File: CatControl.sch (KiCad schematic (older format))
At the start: 4 parts, among them J2 CAT, U2 FT232RL

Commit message: Replace 100 uF caps
The ones I had selected before were only rated for 4V, and I need at least 5V (USB bus).
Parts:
- C16: Manufacturer_Part_Number TPST107M004R0500 -> TACT107M006XTA; Price 0.93 -> 4.4; Vendor Part Number 581-TPST107M004R0500 -> 581-TACT107M006XTA
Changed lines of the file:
@@
 F 1 "100μF" H 5965 1855 50 0000 L CNN
 F 2 "Capacitor_SMD:C_1210_3225Metric" H 5888 1750 50 0001 C CNN
-F 3 "https://www.mouser.com/datasheet/2/40/TPS-2066671.pdf" H 5850 1900 50 0001 C CNN
+F 3 "https://www.mouser.com/datasheet/2/40/tac-776418.pdf" H 5850 1900 50 0001 C CNN
 F 4 "AVX" H 5965 2046 50 0001 C CNN "Manufacturer_Name"
-F 5 "TPST107M004R0500" H 5965 2046 50 0001 C CNN "Manufacturer_Part_Number"
-F 6 "0.93" H 5965 2046 50 0001 C CNN "Price"
-F 7 "581-TPST107M004R0500" H 5965 2046 50 0001 C CNN "Vendor Part Number"
+F 5 "TACT107M006XTA" H 5965 2046 50 0001 C CNN "Manufacturer_Part_Number"
+F 6 "4.4" H 5965 2046 50 0001 C CNN "Price"
+F 7 "581-TACT107M006XTA" H 5965 2046 50 0001 C CNN "Vendor Part Number"
 F 8 "Mouser" H 5965 2046 50 0001 C CNN "Vendor"
 	1    5850 1900

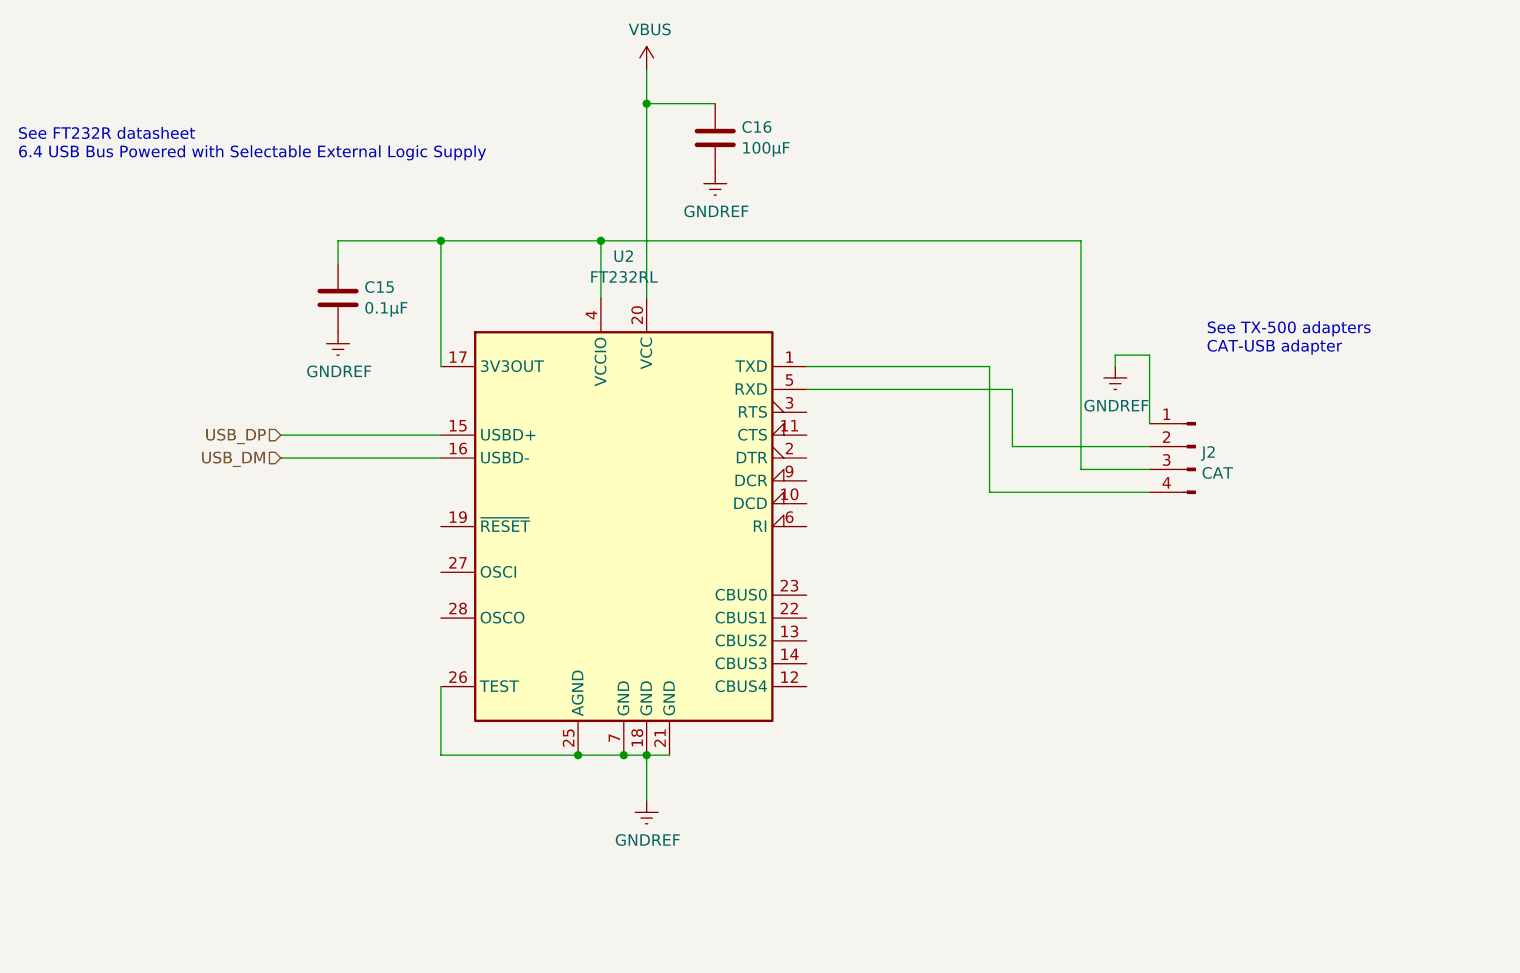
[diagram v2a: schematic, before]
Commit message: Add ID markings on schema and pcb
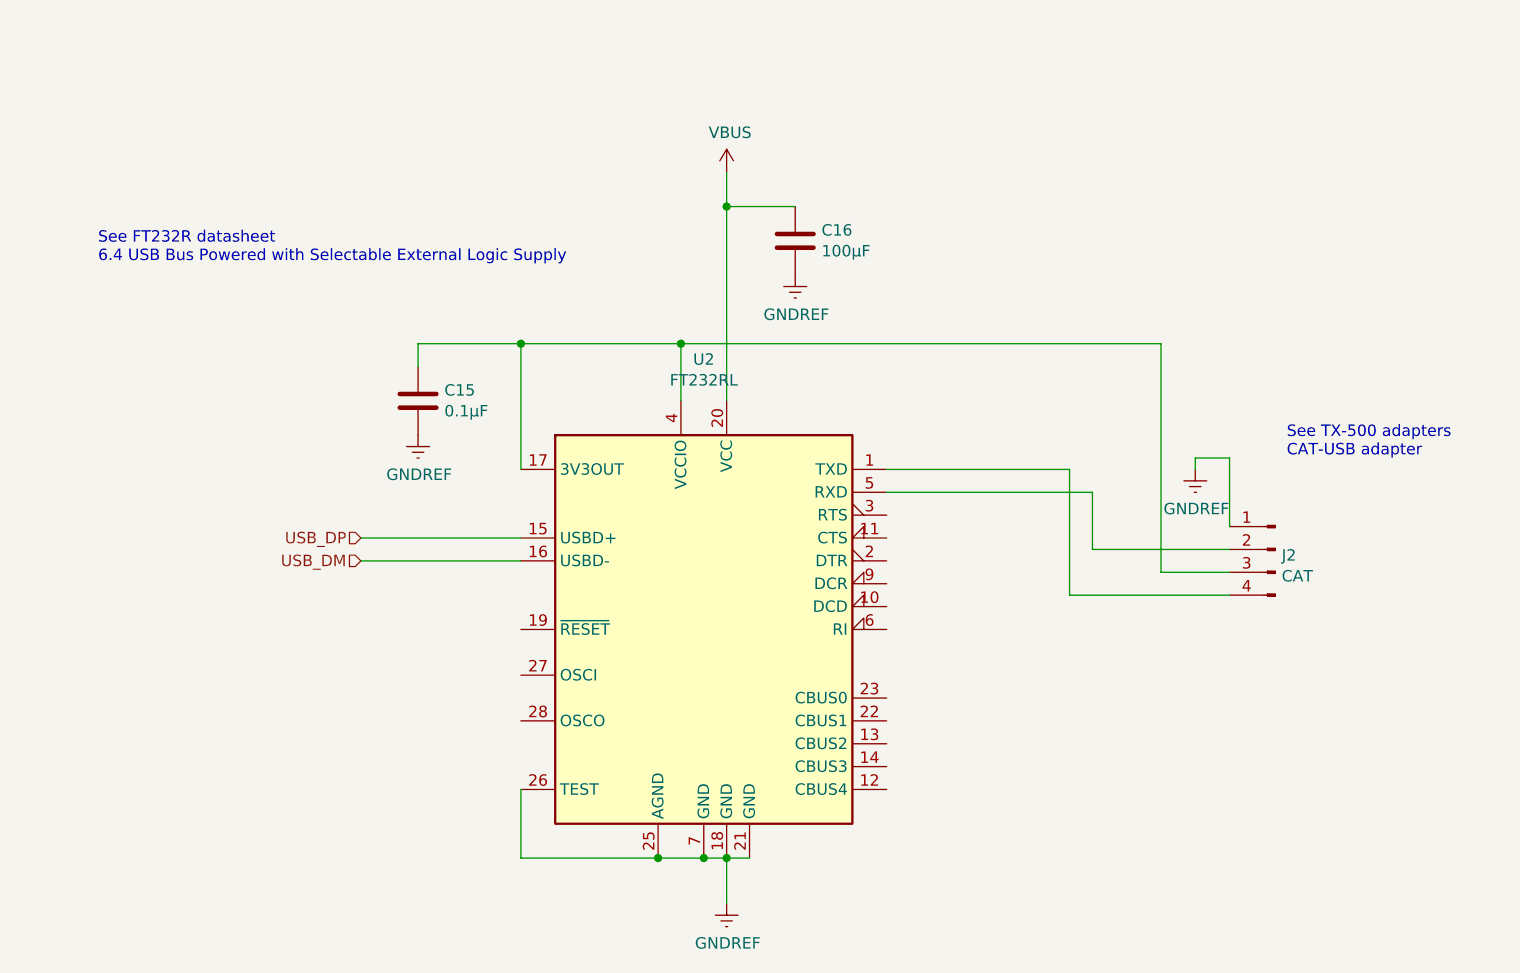
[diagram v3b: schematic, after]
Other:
- moved on the sheet: C15, C16, J2, U2

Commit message: First pass at routing PCB
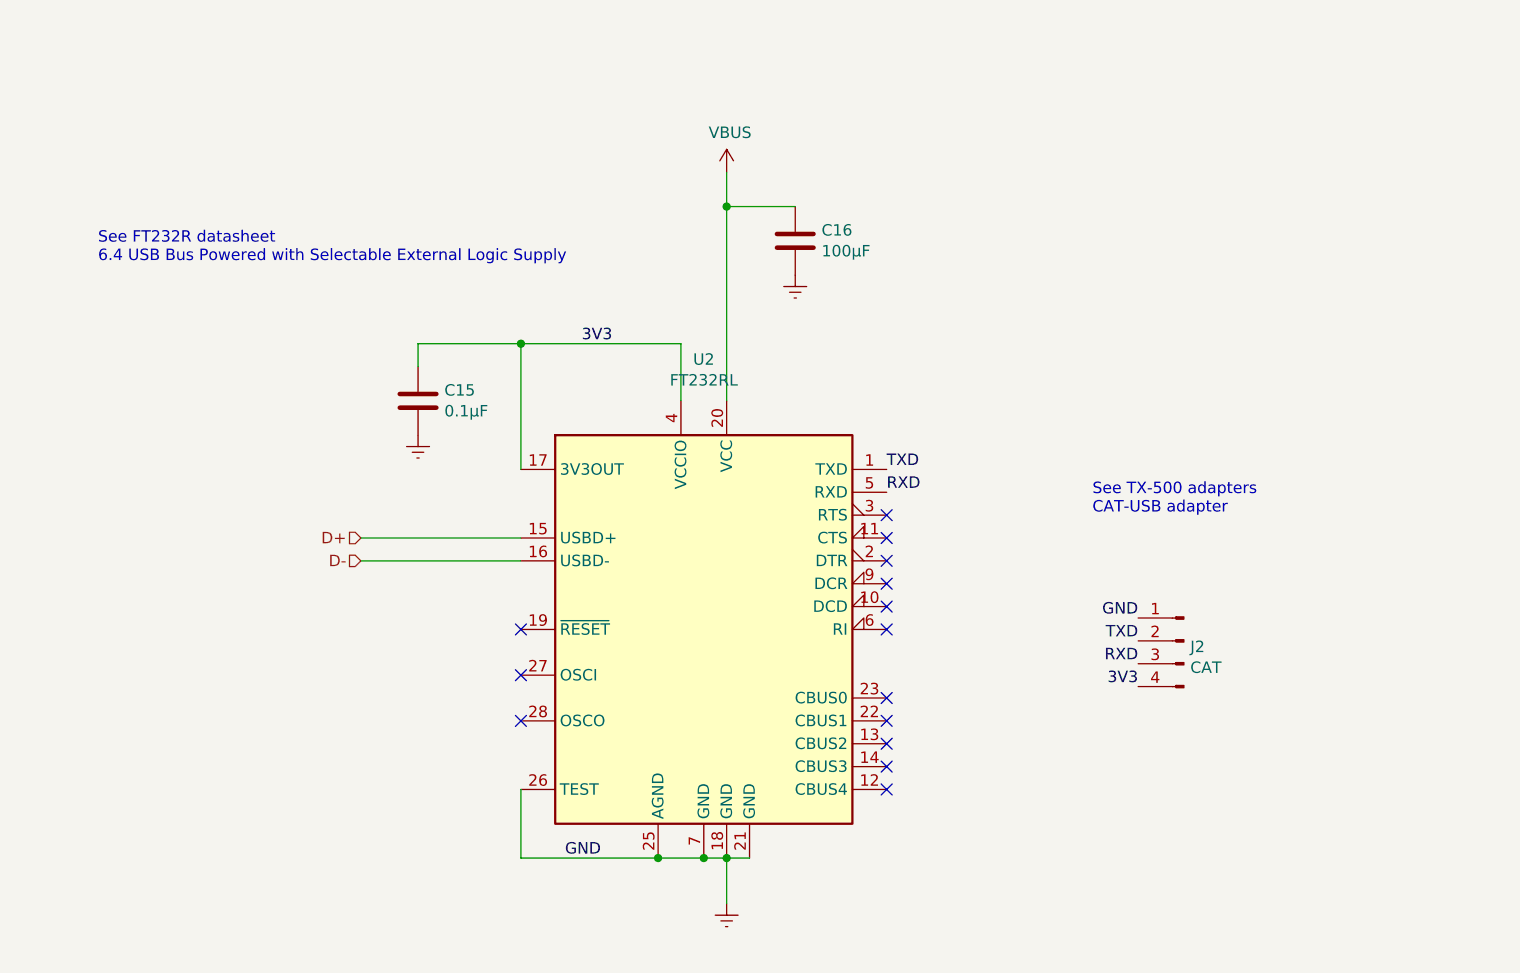
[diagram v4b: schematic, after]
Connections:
- net 3V3: now reaches C15.1, U2.17 (3V3OUT), U2.4 (VCCIO)
- net 3V3: now also J2.4 (Pin_4); no longer J2.3 (Pin_3)
- net TXD: now reaches U2.1 (TXD)
- net TXD: now also J2.2 (Pin_2); no longer J2.4 (Pin_4)
- net RXD: now reaches U2.5 (RXD)
- net RXD: now also J2.3 (Pin_3); no longer J2.2 (Pin_2)
- net USB_DM renamed D-
- net USB_DP renamed D+
- no-connect marks 0 -> 14
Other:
- moved on the sheet: J2
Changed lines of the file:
@@
 Rev "0.1"
 Comp "Chris Keller K0SWE"
-Comment1 ""
+Comment1 "Licensed under Apache-2.0"
 Comment2 ""
 Comment3 ""
@@
 L Connector:Conn_01x04_Male J?
 U 1 1 605A84FC
-P 8300 3700
+P 7900 4100
 AR Path="/605A84FC" Ref="J?"  Part="1"
 AR Path="/6059C0E9/605A84FC" Ref="J2"  Part="1"
-F 0 "J2" H 8272 3674 50  0000 R CNN
-F 1 "CAT" H 8272 3583 50  0000 R CNN
-F 2 "Connector_JST:JST_PH_B4B-PH-SM4-TB_1x04-1MP_P2.00mm_Vertical" H 8300 3700 50  0001 C CNN
-F 3 "https://www.mouser.com/datasheet/2/737/4389_C13924-001_CCP-W20-03-BK-SMT-R-A-1708610.pdf" H 8300 3700 50  0001 C CNN
-F 4 "TX-500 CAT Interconnect" H 8272 3774 50  0001 C CNN "Description"
-F 5 "JST" H 8272 3774 50  0001 C CNN "Manufacturer_Name"
-F 6 "B4B-PH-SM4-TB" H 8272 3774 50  0001 C CNN "Manufacturer_Part_Number"
-F 7 "0.35" H 8272 3774 50  0001 C CNN "Price"
-F 8 "485-4392" H 8272 3774 50  0001 C CNN "Vendor Part Number"
-F 9 "Mouser" H 8272 3774 50  0001 C CNN "Vendor"
-	1    8300 3700
+F 0 "J2" H 7872 4074 50  0000 R CNN
+F 1 "CAT" H 7872 3983 50  0000 R CNN
+F 2 "Connector_JST:JST_PH_B4B-PH-SM4-TB_1x04-1MP_P2.00mm_Vertical" H 7900 4100 50  0001 C CNN
+F 3 "https://www.mouser.com/datasheet/2/737/4389_C13924-001_CCP-W20-03-BK-SMT-R-A-1708610.pdf" H 7900 4100 50  0001 C CNN
+F 4 "TX-500 CAT Interconnect" H 7872 4174 50  0001 C CNN "Description"
+F 5 "JST" H 7872 4174 50  0001 C CNN "Manufacturer_Name"
+F 6 "B4B-PH-SM4-TB" H 7872 4174 50  0001 C CNN "Manufacturer_Part_Number"
+F 7 "0.35" H 7872 4174 50  0001 C CNN "Price"
+F 8 "485-4392" H 7872 4174 50  0001 C CNN "Vendor Part Number"
+F 9 "Mouser" H 7872 4174 50  0001 C CNN "Vendor"
+	1    7900 4100
 	-1   0    0    -1
 $EndComp
@@
 P 5900 5250
 F 0 "#PWR0118" H 5900 5000 50  0001 C CNN
-F 1 "GNDREF" H 5905 5077 50  0000 C CNN
+F 1 "GNDREF" H 5905 5077 50  0001 C CNN
 F 2 "" H 5900 5250 50  0001 C CNN
 F 3 "" H 5900 5250 50  0001 C CNN
 	1    5900 5250
-	1    0    0    -1
-$EndComp
-$Comp
-L power:GNDREF #PWR0119
-U 1 1 605C410A
-P 7950 3350
-F 0 "#PWR0119" H 7950 3100 50  0001 C CNN
-F 1 "GNDREF" H 7955 3177 50  0000 C CNN
-F 2 "" H 7950 3350 50  0001 C CNN
-F 3 "" H 7950 3350 50  0001 C CNN
-	1    7950 3350
 	1    0    0    -1
 $EndComp
@@
 P 6200 2500
 F 0 "#PWR0123" H 6200 2250 50  0001 C CNN
-F 1 "GNDREF" H 6205 2327 50  0000 C CNN
+F 1 "GNDREF" H 6205 2327 50  0001 C CNN
 F 2 "" H 6200 2500 50  0001 C CNN
 F 3 "" H 6200 2500 50  0001 C CNN
@@
 P 4550 3200
 F 0 "#PWR0124" H 4550 2950 50  0001 C CNN
-F 1 "GNDREF" H 4555 3027 50  0000 C CNN
+F 1 "GNDREF" H 4555 3027 50  0001 C CNN
 F 2 "" H 4550 3200 50  0001 C CNN
 F 3 "" H 4550 3200 50  0001 C CNN
@@
 Text Notes 3150 2450 0    50   ~ 0
 See FT232R datasheet\n6.4 USB Bus Powered with Selectable External Logic Supply
-Text Notes 8350 3300 0    50   ~ 0
+Text Notes 7500 3550 0    50   ~ 0
 See TX-500 adapters\nCAT-USB adapter
 Text HLabel 4300 3650 0    50   Input ~ 0
-USB_DP
+D+
 Text HLabel 4300 3750 0    50   Input ~ 0
-USB_DM
+D-
 Wire Wire Line
 	5800 5050 5900 5050
@@
 	5900 5050 5900 5250
 Wire Wire Line
-	6600 3350 7400 3350
-Wire Wire Line
-	7400 3350 7400 3900
-Wire Wire Line
-	7400 3900 8100 3900
-Wire Wire Line
-	6600 3450 7500 3450
-Wire Wire Line
-	7500 3450 7500 3700
-Wire Wire Line
-	7500 3700 8100 3700
-Wire Wire Line
 	5000 3350 5000 2800
 Wire Wire Line
 	5000 2800 5700 2800
-Wire Wire Line
-	7800 2800 7800 3800
-Wire Wire Line
-	7800 3800 8100 3800
-Wire Wire Line
-	8100 3600 8100 3300
-Wire Wire Line
-	8100 3300 7950 3300
-Wire Wire Line
-	7950 3300 7950 3350
 Wire Wire Line
 	5000 4750 5000 5050
@@
 Wire Wire Line
 	5700 2800 5700 3050
-Wire Wire Line
-	5700 2800 7800 2800
 Wire Wire Line
 	5900 2050 5900 2200
@@
 Connection ~ 5600 5050
 Connection ~ 5800 5050
-Connection ~ 5700 2800
 Connection ~ 5900 2200
 Connection ~ 5000 2800
+Text Label 7700 4000 2    50   ~ 0
+GND
+Text Label 7700 4100 2    50   ~ 0
+TXD
+Text Label 7700 4200 2    50   ~ 0
+RXD
+Text Label 7700 4300 2    50   ~ 0
+3V3
+Text Label 5400 2800 2    50   ~ 0
+3V3
+Text Label 6600 3350 0    50   ~ 0
+TXD
+Text Label 6600 3450 0    50   ~ 0
+RXD
+Text Label 5350 5050 2    50   ~ 0
+GND
+NoConn ~ 5000 4050
+NoConn ~ 5000 4250
+NoConn ~ 5000 4450
+NoConn ~ 6600 4750
+NoConn ~ 6600 4650
+NoConn ~ 6600 4550
+NoConn ~ 6600 4450
+NoConn ~ 6600 4350
+NoConn ~ 6600 4050
+NoConn ~ 6600 3950
+NoConn ~ 6600 3850
+NoConn ~ 6600 3750
+NoConn ~ 6600 3650
+NoConn ~ 6600 3550
 $EndSCHEMATC
